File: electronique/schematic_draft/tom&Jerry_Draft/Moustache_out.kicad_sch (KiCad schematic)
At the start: 4 parts, among them J1601 Conn_01x02

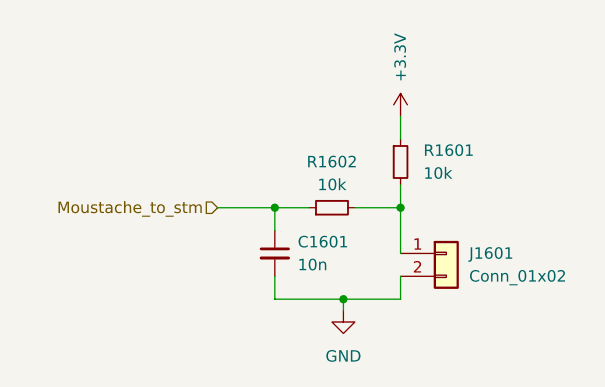
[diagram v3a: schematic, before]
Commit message: Kicad - Deplacement des pins sous PASTE x empreinte MOSFET
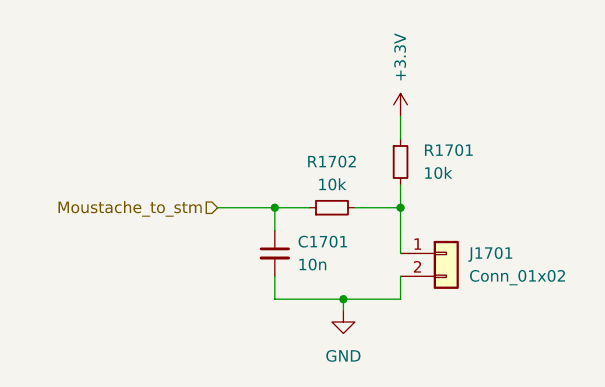
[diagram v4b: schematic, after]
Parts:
- renumbered C1601 to C1701, J1601 to J1701, R1601 to R1701, R1602 to R1702
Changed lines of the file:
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@@
 		(dnp no)
 		(fields_autoplaced yes)
-		(property "Reference" "R1602"
+		(property "Reference" "R1702"
 			(at 143.51 67.31 90)
 			(effects
@@
 			(project "tom&Jerry_Draft"
 				(path "/d6e3fbeb-d028-494d-83bf-2e4a8b12578d/ac7f7f04-c418-4551-b204-a999b9c3c440/4a942aeb-0f5a-4b74-98aa-4f22cccd5125"
+					(reference "R1702")
+					(unit 1)
+				)
+				(path "/d6e3fbeb-d028-494d-83bf-2e4a8b12578d/ac7f7f04-c418-4551-b204-a999b9c3c440/a23499ad-e269-4d60-8a7e-fdf0e52e9311"
+					(reference "R1302")
+					(unit 1)
+				)
+				(path "/d6e3fbeb-d028-494d-83bf-2e4a8b12578d/ac7f7f04-c418-4551-b204-a999b9c3c440/e8ed5780-2114-4427-a772-5bf6fa774e5b"
 					(reference "R1602")
 					(unit 1)
 				)
-				(path "/d6e3fbeb-d028-494d-83bf-2e4a8b12578d/ac7f7f04-c418-4551-b204-a999b9c3c440/a23499ad-e269-4d60-8a7e-fdf0e52e9311"
-					(reference "R1302")
-					(unit 1)
-				)
-				(path "/d6e3fbeb-d028-494d-83bf-2e4a8b12578d/ac7f7f04-c418-4551-b204-a999b9c3c440/e8ed5780-2114-4427-a772-5bf6fa774e5b"
+				(path "/d6e3fbeb-d028-494d-83bf-2e4a8b12578d/ac7f7f04-c418-4551-b204-a999b9c3c440/e9c92678-eab0-4500-8304-4b18da6b06b1"
 					(reference "R1502")
-					(unit 1)
-				)
-				(path "/d6e3fbeb-d028-494d-83bf-2e4a8b12578d/ac7f7f04-c418-4551-b204-a999b9c3c440/e9c92678-eab0-4500-8304-4b18da6b06b1"
-					(reference "R1402")
 					(unit 1)
 				)
@@
 		(dnp no)
 		(fields_autoplaced yes)
-		(property "Reference" "J1601"
+		(property "Reference" "J1701"
 			(at 158.75 77.4699 0)
 			(effects
@@
 			(project "tom&Jerry_Draft"
 				(path "/d6e3fbeb-d028-494d-83bf-2e4a8b12578d/ac7f7f04-c418-4551-b204-a999b9c3c440/4a942aeb-0f5a-4b74-98aa-4f22cccd5125"
+					(reference "J1701")
+					(unit 1)
+				)
+				(path "/d6e3fbeb-d028-494d-83bf-2e4a8b12578d/ac7f7f04-c418-4551-b204-a999b9c3c440/a23499ad-e269-4d60-8a7e-fdf0e52e9311"
+					(reference "J1301")
+					(unit 1)
+				)
+				(path "/d6e3fbeb-d028-494d-83bf-2e4a8b12578d/ac7f7f04-c418-4551-b204-a999b9c3c440/e8ed5780-2114-4427-a772-5bf6fa774e5b"
 					(reference "J1601")
 					(unit 1)
 				)
-				(path "/d6e3fbeb-d028-494d-83bf-2e4a8b12578d/ac7f7f04-c418-4551-b204-a999b9c3c440/a23499ad-e269-4d60-8a7e-fdf0e52e9311"
-					(reference "J1301")
-					(unit 1)
-				)
-				(path "/d6e3fbeb-d028-494d-83bf-2e4a8b12578d/ac7f7f04-c418-4551-b204-a999b9c3c440/e8ed5780-2114-4427-a772-5bf6fa774e5b"
+				(path "/d6e3fbeb-d028-494d-83bf-2e4a8b12578d/ac7f7f04-c418-4551-b204-a999b9c3c440/e9c92678-eab0-4500-8304-4b18da6b06b1"
 					(reference "J1501")
-					(unit 1)
-				)
-				(path "/d6e3fbeb-d028-494d-83bf-2e4a8b12578d/ac7f7f04-c418-4551-b204-a999b9c3c440/e9c92678-eab0-4500-8304-4b18da6b06b1"
-					(reference "J1401")
 					(unit 1)
 				)
@@
 		(dnp no)
 		(fields_autoplaced yes)
-		(property "Reference" "R1601"
+		(property "Reference" "R1701"
 			(at 153.67 66.0399 0)
 			(effects
@@
 			(project "tom&Jerry_Draft"
 				(path "/d6e3fbeb-d028-494d-83bf-2e4a8b12578d/ac7f7f04-c418-4551-b204-a999b9c3c440/4a942aeb-0f5a-4b74-98aa-4f22cccd5125"
+					(reference "R1701")
+					(unit 1)
+				)
+				(path "/d6e3fbeb-d028-494d-83bf-2e4a8b12578d/ac7f7f04-c418-4551-b204-a999b9c3c440/a23499ad-e269-4d60-8a7e-fdf0e52e9311"
+					(reference "R1301")
+					(unit 1)
+				)
+				(path "/d6e3fbeb-d028-494d-83bf-2e4a8b12578d/ac7f7f04-c418-4551-b204-a999b9c3c440/e8ed5780-2114-4427-a772-5bf6fa774e5b"
 					(reference "R1601")
 					(unit 1)
 				)
-				(path "/d6e3fbeb-d028-494d-83bf-2e4a8b12578d/ac7f7f04-c418-4551-b204-a999b9c3c440/a23499ad-e269-4d60-8a7e-fdf0e52e9311"
-					(reference "R1301")
-					(unit 1)
-				)
-				(path "/d6e3fbeb-d028-494d-83bf-2e4a8b12578d/ac7f7f04-c418-4551-b204-a999b9c3c440/e8ed5780-2114-4427-a772-5bf6fa774e5b"
+				(path "/d6e3fbeb-d028-494d-83bf-2e4a8b12578d/ac7f7f04-c418-4551-b204-a999b9c3c440/e9c92678-eab0-4500-8304-4b18da6b06b1"
 					(reference "R1501")
-					(unit 1)
-				)
-				(path "/d6e3fbeb-d028-494d-83bf-2e4a8b12578d/ac7f7f04-c418-4551-b204-a999b9c3c440/e9c92678-eab0-4500-8304-4b18da6b06b1"
-					(reference "R1401")
 					(unit 1)
 				)
@@
 		(dnp no)
 		(fields_autoplaced yes)
-		(property "Reference" "#PWR01602"
+		(property "Reference" "#PWR01702"
 			(at 144.78 90.17 0)
 			(effects
@@
 			(project "tom&Jerry_Draft"
 				(path "/d6e3fbeb-d028-494d-83bf-2e4a8b12578d/ac7f7f04-c418-4551-b204-a999b9c3c440/4a942aeb-0f5a-4b74-98aa-4f22cccd5125"
+					(reference "#PWR01702")
+					(unit 1)
+				)
+				(path "/d6e3fbeb-d028-494d-83bf-2e4a8b12578d/ac7f7f04-c418-4551-b204-a999b9c3c440/a23499ad-e269-4d60-8a7e-fdf0e52e9311"
+					(reference "#PWR01302")
+					(unit 1)
+				)
+				(path "/d6e3fbeb-d028-494d-83bf-2e4a8b12578d/ac7f7f04-c418-4551-b204-a999b9c3c440/e8ed5780-2114-4427-a772-5bf6fa774e5b"
 					(reference "#PWR01602")
 					(unit 1)
 				)
-				(path "/d6e3fbeb-d028-494d-83bf-2e4a8b12578d/ac7f7f04-c418-4551-b204-a999b9c3c440/a23499ad-e269-4d60-8a7e-fdf0e52e9311"
-					(reference "#PWR01302")
-					(unit 1)
-				)
-				(path "/d6e3fbeb-d028-494d-83bf-2e4a8b12578d/ac7f7f04-c418-4551-b204-a999b9c3c440/e8ed5780-2114-4427-a772-5bf6fa774e5b"
+				(path "/d6e3fbeb-d028-494d-83bf-2e4a8b12578d/ac7f7f04-c418-4551-b204-a999b9c3c440/e9c92678-eab0-4500-8304-4b18da6b06b1"
 					(reference "#PWR01502")
-					(unit 1)
-				)
-				(path "/d6e3fbeb-d028-494d-83bf-2e4a8b12578d/ac7f7f04-c418-4551-b204-a999b9c3c440/e9c92678-eab0-4500-8304-4b18da6b06b1"
-					(reference "#PWR01402")
 					(unit 1)
 				)
@@
 		(dnp no)
 		(fields_autoplaced yes)
-		(property "Reference" "C1601"
+		(property "Reference" "C1701"
 			(at 139.7 76.2062 0)
 			(effects
@@
 			(project "tom&Jerry_Draft"
 				(path "/d6e3fbeb-d028-494d-83bf-2e4a8b12578d/ac7f7f04-c418-4551-b204-a999b9c3c440/4a942aeb-0f5a-4b74-98aa-4f22cccd5125"
+					(reference "C1701")
+					(unit 1)
+				)
+				(path "/d6e3fbeb-d028-494d-83bf-2e4a8b12578d/ac7f7f04-c418-4551-b204-a999b9c3c440/a23499ad-e269-4d60-8a7e-fdf0e52e9311"
+					(reference "C1301")
+					(unit 1)
+				)
+				(path "/d6e3fbeb-d028-494d-83bf-2e4a8b12578d/ac7f7f04-c418-4551-b204-a999b9c3c440/e8ed5780-2114-4427-a772-5bf6fa774e5b"
 					(reference "C1601")
 					(unit 1)
 				)
-				(path "/d6e3fbeb-d028-494d-83bf-2e4a8b12578d/ac7f7f04-c418-4551-b204-a999b9c3c440/a23499ad-e269-4d60-8a7e-fdf0e52e9311"
-					(reference "C1301")
-					(unit 1)
-				)
-				(path "/d6e3fbeb-d028-494d-83bf-2e4a8b12578d/ac7f7f04-c418-4551-b204-a999b9c3c440/e8ed5780-2114-4427-a772-5bf6fa774e5b"
+				(path "/d6e3fbeb-d028-494d-83bf-2e4a8b12578d/ac7f7f04-c418-4551-b204-a999b9c3c440/e9c92678-eab0-4500-8304-4b18da6b06b1"
 					(reference "C1501")
-					(unit 1)
-				)
-				(path "/d6e3fbeb-d028-494d-83bf-2e4a8b12578d/ac7f7f04-c418-4551-b204-a999b9c3c440/e9c92678-eab0-4500-8304-4b18da6b06b1"
-					(reference "C1401")
 					(unit 1)
 				)
@@
 		(on_board yes)
 		(dnp no)
-		(property "Reference" "#PWR01601"
+		(property "Reference" "#PWR01701"
 			(at 151.13 66.04 0)
 			(effects
@@
 			(project "tom&Jerry_Draft"
 				(path "/d6e3fbeb-d028-494d-83bf-2e4a8b12578d/ac7f7f04-c418-4551-b204-a999b9c3c440/4a942aeb-0f5a-4b74-98aa-4f22cccd5125"
+					(reference "#PWR01701")
+					(unit 1)
+				)
+				(path "/d6e3fbeb-d028-494d-83bf-2e4a8b12578d/ac7f7f04-c418-4551-b204-a999b9c3c440/a23499ad-e269-4d60-8a7e-fdf0e52e9311"
+					(reference "#PWR01301")
+					(unit 1)
+				)
+				(path "/d6e3fbeb-d028-494d-83bf-2e4a8b12578d/ac7f7f04-c418-4551-b204-a999b9c3c440/e8ed5780-2114-4427-a772-5bf6fa774e5b"
 					(reference "#PWR01601")
 					(unit 1)
 				)
-				(path "/d6e3fbeb-d028-494d-83bf-2e4a8b12578d/ac7f7f04-c418-4551-b204-a999b9c3c440/a23499ad-e269-4d60-8a7e-fdf0e52e9311"
-					(reference "#PWR01301")
-					(unit 1)
-				)
-				(path "/d6e3fbeb-d028-494d-83bf-2e4a8b12578d/ac7f7f04-c418-4551-b204-a999b9c3c440/e8ed5780-2114-4427-a772-5bf6fa774e5b"
+				(path "/d6e3fbeb-d028-494d-83bf-2e4a8b12578d/ac7f7f04-c418-4551-b204-a999b9c3c440/e9c92678-eab0-4500-8304-4b18da6b06b1"
 					(reference "#PWR01501")
 					(unit 1)
 				)
-				(path "/d6e3fbeb-d028-494d-83bf-2e4a8b12578d/ac7f7f04-c418-4551-b204-a999b9c3c440/e9c92678-eab0-4500-8304-4b18da6b06b1"
-					(reference "#PWR01401")
-					(unit 1)
-				)
